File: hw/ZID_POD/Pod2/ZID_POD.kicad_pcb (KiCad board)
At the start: 2 copper layers, 52.8 x 19.3 mm, 2 parts, among them J1 Z80-POD (2)

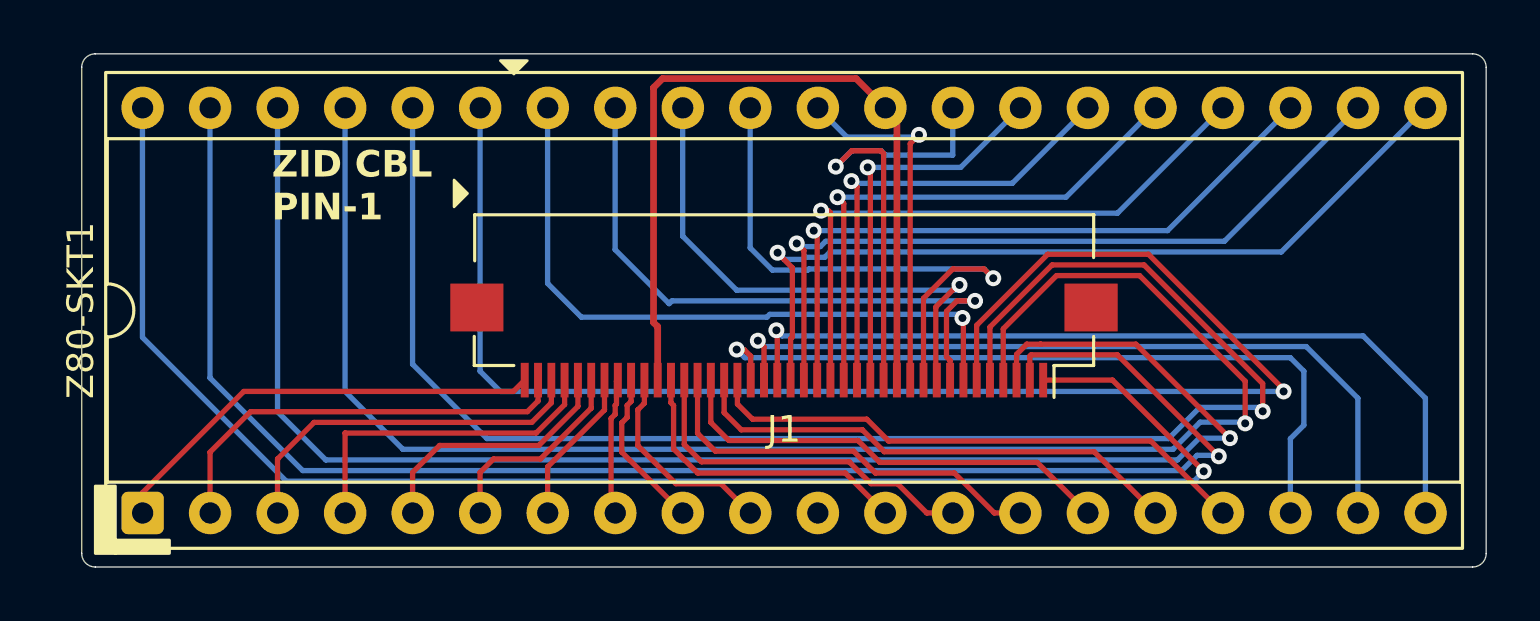
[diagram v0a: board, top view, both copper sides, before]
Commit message: PCB: Ready to order - ZID, POD1, POD2, POD3, POD4, ExpBP
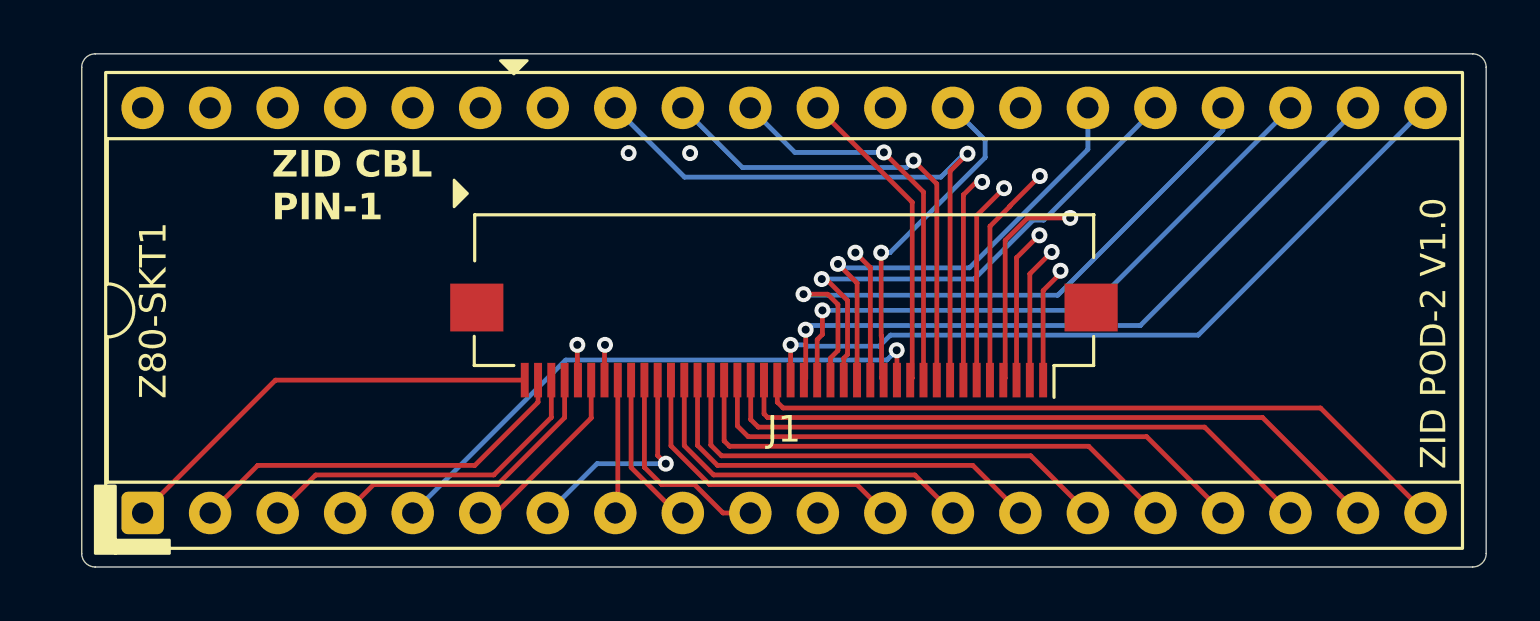
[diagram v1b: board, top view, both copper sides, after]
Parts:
- J1: value Z80-POD (2) -> FFC/FPC-40 Socket
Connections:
- J1 pad 12: /GND -> /A15
- J1 pad 30: /GND -> /D4
- J1 pad 34: /D4 -> /GND
- J1 pad 36: /A15 -> /GND
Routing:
- net /A5: track 57.3 -> 29.2 mm
- net /GND: track 30.2 -> 2.64 mm, vias 0 -> 4
- net /A6: track 59.4 -> 34.6 mm
- net /A7: track 61.0 -> 37.8 mm
- net /A8: track 59.0 -> 37.1 mm
- net /A9: track 59.4 -> 39.7 mm
- net /A10: track 58.4 -> 42.0 mm
- net /A15: track 9.76 -> 21.9 mm, vias 0 -> 1
- net /M1-: track 14.7 -> 21.9 mm
- net /A1: track 21.2 -> 14.9 mm
- net /HALT-: track 28.8 -> 23.2 mm, vias 1 -> 0
- net /IORQ-: track 31.7 -> 26.9 mm, vias 1 -> 0
- net /RFSH-: track 17.1 -> 12.6 mm
- net /MREQ-: track 29.4 -> 25.2 mm, vias 1 -> 0
- net /RD-: track 31.9 -> 28.9 mm
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- added copper zone on In1.Cu, net /GND
- added copper zone on In2.Cu, net /GND
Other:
- copper layers 2 -> 4
- board text added: "ZID POD-2 V1.0"
